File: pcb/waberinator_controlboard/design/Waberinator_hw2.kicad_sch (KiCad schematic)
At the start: 96 parts, among them J2 Strang 2, J3 Strang 1, J4 Strang 3, J5 Strang 4, J6 Strang 5, J7 Strang 6, J8 Conn_01x08_Pin, J9 Conn_01x04_Pin, Q1 AOSP21321, Q2 SISHA04DN-T1-GE3, Q3 SISHA04DN-T1-GE3, Q4 SISHA04DN-T1-GE3, Q5 SISHA04DN-T1-GE3, Q6 SISHA04DN-T1-GE3, Q7 SISHA04DN-T1-GE3, SW1 SW_SPST, SW2 SW_SPST, U1 LM75B, U2 LM73606QRNPRQ1, U3 AMS1117-3.3, U3 MCP14A0304xMNY, U4 MCP14A0304xMNY, U6 MCP14A0304xMNY, U7 STM32F030R8Tx

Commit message: add lichterkette
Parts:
- removed FL1: ~, g7_emi:CMC_Laird_CM2021Y330R-10, symbol Device:EMI_Filter_LL_1423
- removed SW1, SW2: SW_SPST, symbol Switch:SW_SPST
- added C33: 10µF, Capacitor_SMD:C_1210_3225Metric_Pad1.33x2.70mm_HandSolder, symbol Device:C
- added FB1, FB2, FB4, FB5: FerriteBead, Capacitor_SMD:C_1210_3225Metric_Pad1.33x2.70mm_HandSolder, symbol Device:FerriteBead
- added J10, J2, J3, J5, J6, J7, J8, J9: preconf. cable, symbol Connector:Conn_01x01_Pin
- added R12, R13, R14, R15, R20: 100, Resistor_SMD:R_0603_1608Metric_Pad0.98x0.95mm_HandSolder, symbol Device:R
- added R4: 100k, Resistor_SMD:R_0603_1608Metric_Pad0.98x0.95mm_HandSolder, symbol Device:R
- added SW1, SW2: SW_SPDT, g7_hmi:switch_800usp8p1a1m6re, symbol Switch:SW_SPDT
- C10: renamed from C21; Digikey P16502TR-ND -> P16502CT-ND
- C12: renamed from C5; footprint (none) -> Capacitor_SMD:C_1210_3225Metric_Pad1.33x2.70mm_HandSolder
- C31: renamed from C22; Digikey P16502TR-ND -> P16502CT-ND
- C32: renamed from C25; Digikey P16502TR-ND -> P16502CT-ND
- D7: Digikey 976-BXFN-27G-21L-3C4-00-0-3TR-ND -> 976-BXFN-27G-21L-3C4-00-0-3CT-ND
- FB3: renamed from FB1; footprint (none) -> Capacitor_SMD:C_1210_3225Metric_Pad1.33x2.70mm_HandSolder
- L1: Digikey SRU1048-4R7YTR-ND -> SRU1048-4R7YCT-ND
- Q2: renamed from Q3; footprint (none) -> Package_TO_SOT_SMD:LFPAK33
- Q3: renamed from Q2; footprint (none) -> Package_TO_SOT_SMD:LFPAK33
- Q4, Q5, Q6, Q7: footprint (none) -> Package_TO_SOT_SMD:LFPAK33
- RV1: renamed from RV3; footprint (none) -> g7_hmi:poti_3310C-025-103L; Digikey 987-1714-ND -> 118-3310C-025-103L-ND
- RV2: renamed from RV1; footprint (none) -> g7_hmi:poti_3310C-025-103L; Digikey 987-1714-ND -> 118-3310C-025-103L-ND
- RV3: renamed from RV2; footprint (none) -> g7_hmi:poti_3310C-025-103L; Digikey 987-1714-ND -> 118-3310C-025-103L-ND
- U3: renamed from U2; Digikey 296-49519-2-ND -> 296-49519-1-ND
- U4: renamed from U1; Digikey 568-4688-2-ND -> 568-4688-1-ND
- U5: renamed from U3; Digikey MCP14A0304T-E/SNTR-ND -> MCP14A0304T-E/SNCT-ND
- U6: renamed from U4; Digikey MCP14A0304T-E/SNTR-ND -> MCP14A0304T-E/SNCT-ND
- U7: renamed from U6; Digikey MCP14A0304T-E/SNTR-ND -> MCP14A0304T-E/SNCT-ND
- renumbered C2 to C1, C20 to C11, C18 to C13, C16 to C14, C14 to C15, C15 to C16, C19 to C18, C13 to C19, C4 to C2, C1 to C20, C9 to C21, C3 to C22, C24 to C23, C26 to C24, C28 to C25, C30 to C26, C23 to C27, C27 to C28, C5 to C3, C31 to C30, C6 to C4, C7 to C5, C8 to C6, C12 to C7, C10 to C8, C11 to C9, J9 to J1, J3 to J11, J2 to J12, J4 to J13, J5 to J14, J6 to J15, J7 to J16, J8 to J4, R22 to R1, R5 to R11, R23 to R2, R1 to R21, R3 to R22, R4 to R23, R11 to R24, R2 to R25, R12 to R26, R13 to R27, R14 to R28, R15 to R29, R21 to R3, R20 to R30, R6 to R5, R7 to R6, R8 to R7, R9 to R8, R10 to R9, U7 to U1, U3 to U2
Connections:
- net +3.3VA: now also SW1.1 (A), SW2.1 (A)
- net DC_IN+: now also FB1.1
- net DC_IN-: now also FB2.1
- net DC_prefuse: now also FB1.2
- net DC_prot: now also FB4.1; no longer C10.1, C11.1, C13.1, U3.20 (VIN), U3.21 (VIN), U3.22 (VIN)
- net RET: now also C33.2, FB2.2, R4.1, SW1.3 (C), SW2.3 (C)
- net VLed: now also C33.1, FB5.2; no longer C22.1, C23.1, C27.1, C31.1, C32.1, L1.2, R22.1, U3.8 (BIAS)
- net adc_brightness: now also R12.1; no longer RV1.2
- net adc_depth: now also R20.1; no longer RV3.2
- net adc_frequency: now also R13.1; no longer RV2.2
- net button1: now also R14.1
- net button2: now also R15.1
- net boot0: now reaches U1.60 (BOOT0)
- net boot0: now also R4.2
- new net: R13.2, RV2.2
- new net: R20.2, RV3.2
- new net: R14.2, SW1.2 (B)
- new net: C10.1, C11.1, C13.1, FB4.2, U3.20 (VIN), U3.21 (VIN), U3.22 (VIN)
- new net: R12.2, RV1.2
- new net: R15.2, SW2.2 (B)
- new net lm76606_out: C22.1, C23.1, C27.1, C31.1, C32.1, FB5.1, L1.2, R22.1, U3.8 (BIAS)
- no-connect marks 2 -> 4
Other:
- note removed: "Teilenummern für vorkonfektionierte Kab"
- moved on the sheet: C14, C15, C16

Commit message: [PCB] components roughly placed
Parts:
- removed C24, C25, C26: 1µF, Capacitor_SMD:C_0603_1608Metric_Pad1.08x0.95mm_HandSolder, symbol Device:C
- removed C28, C29, C30: 100nF, Capacitor_SMD:C_0603_1608Metric_Pad1.08x0.95mm_HandSolder, symbol Device:C
- removed D3: LED, LED_THT:LED_D3.0mm_Horizontal_O1.27mm_Z2.0mm, symbol Device:LED
- removed J10, J5, J6, J7, J8, J9: preconf. cable, symbol Connector:Conn_01x01_Pin
- removed J11: Strang 1, Connector_JST:JST_XH_B2B-XH-AM_1x02_P2.50mm_Vertical, symbol Connector_Generic:Conn_01x02
- removed J12: Strang 2, Connector_JST:JST_XH_B2B-XH-AM_1x02_P2.50mm_Vertical, symbol Connector_Generic:Conn_01x02
- removed J13: Strang 3, Connector_JST:JST_XH_B2B-XH-AM_1x02_P2.50mm_Vertical, symbol Connector_Generic:Conn_01x02
- removed J14: Strang 4, Connector_JST:JST_XH_B2B-XH-AM_1x02_P2.50mm_Vertical, symbol Connector_Generic:Conn_01x02
- removed J15: Strang 5, Connector_JST:JST_XH_B2B-XH-AM_1x02_P2.50mm_Vertical, symbol Connector_Generic:Conn_01x02
- removed J16: Strang 6, Connector_JST:JST_XH_B2B-XH-AM_1x02_P2.50mm_Vertical, symbol Connector_Generic:Conn_01x02
- removed Q2, Q3, Q4, Q5, Q6, Q7: SISHA04DN-T1-GE3, Package_TO_SOT_SMD:LFPAK33, symbol Device:Q_NMOS_GDS
- removed R15: 100, Resistor_SMD:R_0603_1608Metric_Pad0.98x0.95mm_HandSolder, symbol Device:R
- removed R19: R, Resistor_SMD:R_0603_1608Metric_Pad0.98x0.95mm_HandSolder, symbol Device:R
- removed R24, R25, R26, R27, R28, R29: 1, Resistor_SMD:R_0603_1608Metric_Pad0.98x0.95mm_HandSolder, symbol Device:R
- removed SW2: SW_SPDT, g7_hmi:switch_800usp8p1a1m6re, symbol Switch:SW_SPDT
- removed U5, U6, U7: MCP14A0304xMNY, Package_SO:SOIC-8_3.9x4.9mm_P1.27mm, symbol Driver_FET:MCP14A0304xMNY
- added H1, H2, H3, H4: MountingHole, MountingHole:MountingHole_3.2mm_M3_DIN965, symbol Mechanical:MountingHole
- renumbered C13 to C12, C14 to C13, C15 to C14, C16 to C15, C17 to C16, C18 to C17, C19 to C18, C20 to C19, C21 to C20, C22 to C21, C23 to C22, C27 to C23, C31 to C24, C32 to C25, C33 to C26, C12 to CVCC1, R12 to R11, R13 to R12, R14 to R13, R16 to R15, R17 to R16, R18 to R17, R20 to R19, R21 to R20, R22 to R21, R23 to R22, R30 to R23, R11 to RT1
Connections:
- net lm_fb: now reaches C21.2, R21.2, R22.1, U3.11 (FB)
- net lm_vin: now reaches C10.1, C11.1, C12.1, FB4.2, U3.20 (VIN), U3.21 (VIN), U3.22 (VIN)
- net lm_rt: now reaches RT1.2, U3.9 (RT)
- net lm_sw: now reaches C19.2, L1.1, U3.1 (SW), U3.2 (SW), U3.3 (SW), U3.4 (SW), U3.5 (SW)
- net lm_vcc: now reaches CVCC1.1, U3.7 (VCC)
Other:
- added sheet Two Strings (two_strings.kicad_sch)
- added sheet Two Strings1 (two_strings.kicad_sch)
- added sheet Two Strings2 (two_strings.kicad_sch)

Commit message: [HW] draft chassis
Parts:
- removed D4, D5, D6: LED, LED_THT:LED_D3.0mm_Horizontal_O1.27mm_Z2.0mm, symbol Device:LED
- added D3: RGB LED, LED_THT:LED_D5.0mm-4_RGB_Wide_Pins, symbol Device:LED_BRKG
- added J17: 4 Pole Chassis Connector, g7_connectors:Chassis_Connector, symbol Connector:Conn_01x01_Pin
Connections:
- net RET: now also D3.3 (K)
- net at R16.2: now also D3.4 (GA)
- net at R17.2: now also D3.2 (RA)
- net at R15.2: now also D3.1 (BA)
- net button2: no longer names the net of U1.30 (PB11)
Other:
- moved on the sheet: R13, R16, R17, SW1

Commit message: [HW] moved lights connector to top
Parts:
- removed NT1: NetTie_2, NetTie:NetTie-2_SMD_Pad0.5mm, symbol Device:NetTie_2
- removed R1, R2: 100, Resistor_SMD:R_0603_1608Metric_Pad0.98x0.95mm_HandSolder, symbol Device:R
- added FB6: FerriteBead, Capacitor_SMD:C_1210_3225Metric_Pad1.33x2.70mm_HandSolder, symbol Device:FerriteBead
- added J18, J19, J20, J21, J22, J23, J24, J25, J26: GX12-4, g7_connectors:gx12_sleeve, symbol Connector:Conn_01x01_Pin
- J17: value 4 Pole Chassis Connector -> GX16-4
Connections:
- net RET: now also FB6.2
- net bat_kelvin+: now reaches R5.2
- net bat_kelvin+: now also J1.3 (Pin_3)
- net bat_kelvin-: now reaches J1.4 (Pin_4)
- net bat_kelvin-: now also FB6.1
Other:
- note added: "Waberinator"
- note added: "battery"
- note added: "lights"
- moved on the sheet: C13, C14, C15, C8, D2, D3, J17, J4, R11, R12, R13, R15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

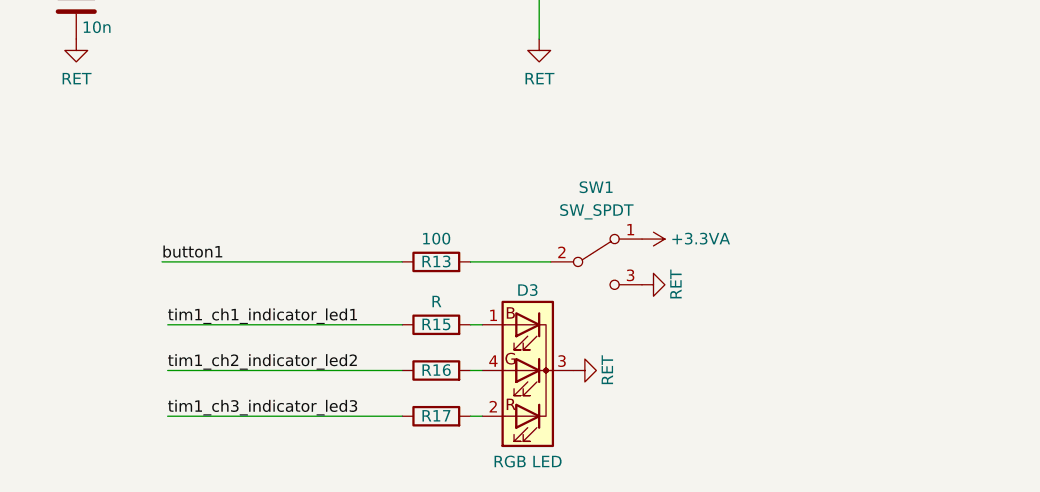
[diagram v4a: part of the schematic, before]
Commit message: [HW] pcb production ready
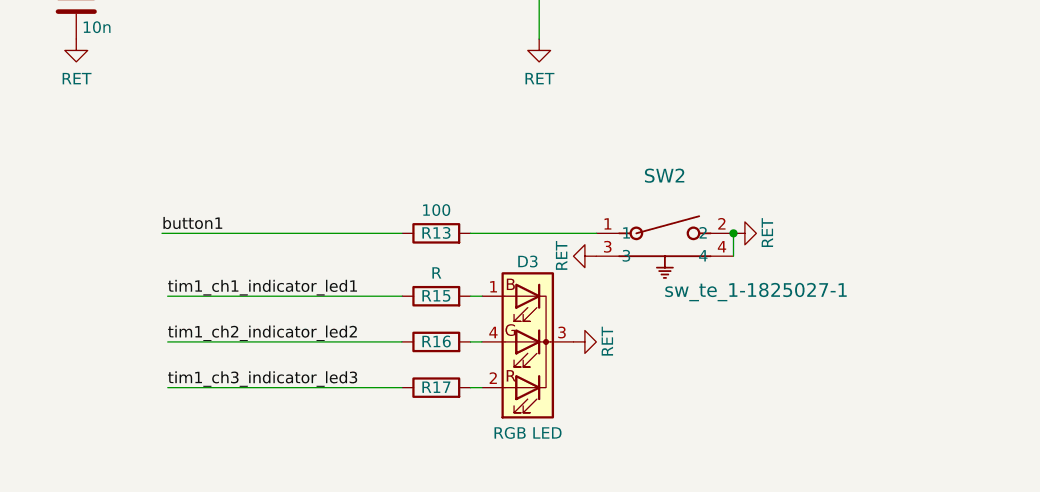
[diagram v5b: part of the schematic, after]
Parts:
- removed SW1: SW_SPDT, g7_hmi:switch_800usp8p1a1m6re, symbol Switch:SW_SPDT
- added SW2: sw_te_1-1825027-1, g7_hmi:sw_te_1-1825027-1, symbol g7_hmi:sw_te_1-1825027-1
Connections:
- net RET: now also SW2.2, SW2.3, SW2.4
- net at R13.2: now also SW2.1
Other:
- moved on the sheet: D3, R13, R15, R16, R17

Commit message: [HW] finish layout
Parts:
- R23: Digikey RMCF1210JT1R00TR-ND -> RMCF1210JT1R00CT-ND
- SW2: Digikey (none) -> 450-1658-ND
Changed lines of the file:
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@@
       (effects (font (size 1.27 1.27)) hide)
     )
-    (property "Digikey" "RMCF1210JT1R00TR-ND" (at 370.205 246.38 0)
+    (property "Digikey" "RMCF1210JT1R00CT-ND" (at 370.205 246.38 0)
       (effects (font (size 1.27 1.27)) hide)
     )
@@
       (effects (font (size 1.27 1.27) italic) hide)
     )
+    (property "Digikey" "450-1658-ND" (at 208.28 234.95 0)
+      (effects (font (size 1.27 1.27)) hide)
+    )
     (pin "4")

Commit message: [HW] misc adjustments to mechanics
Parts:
- added D4: SD103CW-E3-08, Diode_SMD:D_SOD-123, symbol Device:D_Schottky
- J17, J18, J19, J20, J21, J22, J23, J24, J25, J26: now left out of the parts list
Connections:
- net bat_kelvin+: now also D4.2 (A); no longer R5.2
- new net: D4.1 (K), R5.2
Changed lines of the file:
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@@
     (stroke (width 0) (type default))
   )
+  (wire (pts (xy 78.74 45.72) (xy 83.82 45.72))
+    (stroke (width 0) (type default))
+  )
   (wire (pts (xy 46.355 213.36) (xy 64.77 213.36))
     (stroke (width 0) (type default))
@@
     (stroke (width 0) (type default))
   )
-  (wire (pts (xy 25.4 45.72) (xy 83.82 45.72))
+  (wire (pts (xy 25.4 45.72) (xy 71.12 45.72))
     (stroke (width 0) (type default))
   )
@@
   )
   (symbol (lib_id "Connector:Conn_01x01_Pin") (at 354.33 179.07 0) (mirror y) (unit 1)
-    (in_bom yes) (on_board yes) (dnp no) (fields_autoplaced)
+    (in_bom no) (on_board no) (dnp no) (fields_autoplaced)
     (property "Reference" "J19" (at 353.695 173.99 0)
       (effects (font (size 1.27 1.27)))
@@
   )
   (symbol (lib_id "Connector:Conn_01x01_Pin") (at 377.19 158.75 0) (mirror y) (unit 1)
-    (in_bom yes) (on_board yes) (dnp no) (fields_autoplaced)
+    (in_bom no) (on_board no) (dnp no) (fields_autoplaced)
     (property "Reference" "J21" (at 376.555 153.67 0)
       (effects (font (size 1.27 1.27)))
@@
   )
   (symbol (lib_id "Connector:Conn_01x01_Pin") (at 354.33 195.58 0) (mirror y) (unit 1)
-    (in_bom yes) (on_board yes) (dnp no) (fields_autoplaced)
+    (in_bom no) (on_board no) (dnp no) (fields_autoplaced)
     (property "Reference" "J24" (at 353.695 190.5 0)
       (effects (font (size 1.27 1.27)))
@@
   )
   (symbol (lib_id "Connector:Conn_01x01_Pin") (at 323.85 179.07 0) (unit 1)
-    (in_bom yes) (on_board yes) (dnp no)
+    (in_bom no) (on_board no) (dnp no)
     (property "Reference" "J17" (at 324.485 173.99 0)
       (effects (font (size 1.27 1.27)))
@@
   )
   (symbol (lib_id "Connector:Conn_01x01_Pin") (at 354.33 162.56 0) (mirror y) (unit 1)
-    (in_bom yes) (on_board yes) (dnp no) (fields_autoplaced)
+    (in_bom no) (on_board no) (dnp no) (fields_autoplaced)
     (property "Reference" "J18" (at 353.695 157.48 0)
       (effects (font (size 1.27 1.27)))
@@
   )
   (symbol (lib_id "Connector:Conn_01x01_Pin") (at 377.19 182.88 0) (mirror y) (unit 1)
-    (in_bom yes) (on_board yes) (dnp no) (fields_autoplaced)
+    (in_bom no) (on_board no) (dnp no) (fields_autoplaced)
     (property "Reference" "J23" (at 376.555 177.8 0)
       (effects (font (size 1.27 1.27)))
@@
     )
   )
+  (symbol (lib_id "Device:D_Schottky") (at 74.93 45.72 180) (unit 1)
+    (in_bom yes) (on_board yes) (dnp no) (fields_autoplaced)
+    (property "Reference" "D4" (at 75.2475 39.37 0)
+      (effects (font (size 1.27 1.27)))
+    )
+    (property "Value" "SD103CW-E3-08" (at 75.2475 41.91 0)
+      (effects (font (size 1.27 1.27)))
+    )
+    (property "Footprint" "Diode_SMD:D_SOD-123" (at 74.93 45.72 0)
+      (effects (font (size 1.27 1.27)) hide)
+    )
+    (property "Datasheet" "~" (at 74.93 45.72 0)
+      (effects (font (size 1.27 1.27)) hide)
+    )
+    (property "MPN" "SD103CW-E3-08" (at 74.93 45.72 0)
+      (effects (font (size 1.27 1.27)) hide)
+    )
+    (pin "1")
+    (pin "2")
+    (instances
+      (project "Waberinator_hw2"
+        (path "/2abe1fd5-5254-4661-ace0-8064915e9450"
+          (reference "D4") (unit 1)
+        )
+      )
+    )
+  )
   (symbol (lib_id "g7_power_symbols:RET") (at 74.295 31.75 0) (unit 1)
     (in_bom yes) (on_board yes) (dnp no) (fields_autoplaced)
@@
   )
   (symbol (lib_id "Connector:Conn_01x01_Pin") (at 377.19 175.26 0) (mirror y) (unit 1)
-    (in_bom yes) (on_board yes) (dnp no) (fields_autoplaced)
+    (in_bom no) (on_board no) (dnp no) (fields_autoplaced)
     (property "Reference" "J20" (at 376.555 170.18 0)
       (effects (font (size 1.27 1.27)))
@@
   )
   (symbol (lib_id "Connector:Conn_01x01_Pin") (at 377.19 191.77 0) (mirror y) (unit 1)
-    (in_bom yes) (on_board yes) (dnp no) (fields_autoplaced)
+    (in_bom no) (on_board no) (dnp no) (fields_autoplaced)
     (property "Reference" "J25" (at 376.555 186.69 0)
       (effects (font (size 1.27 1.27)))
@@
   )
   (symbol (lib_id "Connector:Conn_01x01_Pin") (at 377.19 166.37 0) (mirror y) (unit 1)
-    (in_bom yes) (on_board yes) (dnp no) (fields_autoplaced)
+    (in_bom no) (on_board no) (dnp no) (fields_autoplaced)
     (property "Reference" "J22" (at 376.555 161.29 0)
       (effects (font (size 1.27 1.27)))
@@
   )
   (symbol (lib_id "Connector:Conn_01x01_Pin") (at 377.19 199.39 0) (mirror y) (unit 1)
-    (in_bom yes) (on_board yes) (dnp no) (fields_autoplaced)
+    (in_bom no) (on_board no) (dnp no) (fields_autoplaced)
     (property "Reference" "J26" (at 376.555 194.31 0)
       (effects (font (size 1.27 1.27)))
